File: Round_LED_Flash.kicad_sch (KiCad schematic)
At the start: 65 parts, among them J1 USB4085-GF-A, J2 BATTERY, Q20 AO3401A, Q21 AO3401A, Q22 2N7002-7-F, Q23 2N7002-7-F, SW1 POWER, SW2 SHUTTER, U10 ESP32-C3-WROOM-02-N4, U6 TPS63070RNMR

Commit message: Preserve balanced supercapacitor charger draft before completion
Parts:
- removed C31, C33: 5F 2.7V, Capacitor_THT:CP_Radial_D10.0mm_P5.00mm, symbol Device:C_Polarized
- removed R31, R32: 2.2k, Resistor_SMD:R_0603_1608Metric, symbol Device:R
- added C60: 4.7u 10V, Capacitor_SMD:C_0805_2012Metric, symbol Device:C
- added C61: 2.2u 16V, Capacitor_SMD:C_0805_2012Metric, symbol Device:C
- added Q30: AO3401A, Package_TO_SOT_SMD:SOT-23, symbol Transistor_FET:Q_PMOS_GSD
- added Q31, Q32, Q33: MMBT3904-7-F, Package_TO_SOT_SMD:SOT-23, symbol Transistor_BJT:Q_NPN_BEC
- added R52, R53, R60, R64, R65, R66, R67: 100k, Resistor_SMD:R_0603_1608Metric, symbol Device:R
- added R61: 24k, Resistor_SMD:R_0603_1608Metric, symbol Device:R
- added R62, R63: 10k, Resistor_SMD:R_0603_1608Metric, symbol Device:R
- added R68, R69: 47k, Resistor_SMD:R_0603_1608Metric, symbol Device:R
- added U30: LTC3225EDDB#TRMPBF, Package_DFN_QFN:DFN-10-1EP_2x3mm_P0.5mm_EP0.64x2.4mm, symbol Round_LED_Flash:LTC3225
- Q22, Q23: value 2N7002-7-F -> MMBT3904-7-F; symbol Transistor_FET:Q_NMOS_GSD -> Transistor_BJT:Q_NPN_BEC; BOM Comments Lifecycle/orderable suffix must be rechecked before BOM fre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 -> (none); MPN 2N7002-7-F -> MMBT3904-7-F
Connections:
- net 3V3: now also R62.1
- net ARM: now also R67.1
- net BAT_PROT: now also C60.1, Q30.2 (S), Q31.1 (B), R60.1, R67.2, U30.9 (VIN)
- net CAP_BANK: now also U30.10 (COUT)
- net CAP_MID: now also U30.3 (CX)
- net GND: now also C60.2, Q31.2 (E), Q32.2 (E), Q33.2 (E), R61.2, R64.2, R65.2, R66.2, U30.11 (EP_GND), U30.6 (VSEL), U30.8 (GND)
- net LOGIC_PG: now also R52.1, R53.1; no longer Q22.1 (G), Q23.1 (G)
- net VBUS_RAW: now also R65.1, R69.1
- new net CAP_CHG_EN: Q32.3 (C), Q33.3 (C), R63.2, R64.1, U30.4 (SHDN)
- new net CAP_EN_FEED: Q30.3 (D), R63.1
- new net CAP_EN_GATE: Q30.1 (G), Q31.3 (C), R60.2
- new net CAP_FLY_N: C61.2, U30.2 (C_MINUS)
- new net CAP_FLY_P: C61.1, U30.1 (C_PLUS)
- new net CAP_PGOOD: R62.2, U30.5 (PGOOD)
- new net CAP_PROG: R61.1, U30.7 (PROG)
- new net HW_WINDOW: R66.1, R68.1
- new net Q32_BASE: Q32.1 (B), R68.2
- new net Q33_BASE: Q33.1 (B), R69.2
- new net SENSE_BASE_0: Q22.1 (B), R52.2
- new net SENSE_BASE_1: Q23.1 (B), R53.2
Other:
- note added: "03 / 2.5 F EFFECTIVE CAP BANK - regulated 4.8 V"
- note added: "08 / 4.8 V SUPERCAP CHARGER + AUTOMATIC BALANCING"
- note added: "Charge enabled by ARM; USB presence or timed flash window forces SHDN low."
- note added: "Nominal stored energy 28.8 J. Flash isolation and service discharge still pending."
- note added: "Two series cells; midpoint connects to LTC3225 CX. No bleed balancing resistors."
- note added: "hardware pulse cutoff/re-arm, flash isolation/discharge, exact MPNs, routing,"
- note removed: "03 / 5 F EFFECTIVE CAP BANK - 5.4 V nominal rating"
- note removed: "INCOMPLETE: add limited reverse-blocking charger, per-section clamps and flash isolation."
- note removed: "Maximum charge is one protected Li-ion cell. Stored energy at 4.2 V = 44.1 J."
- note removed: "hardware pulse cutoff/re-arm, cap balancing/isolation, exact MPNs, routing,"

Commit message: Complete prototype circuit candidate with protected power and bounded flash control
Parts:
- added C1, C140, C141, C142, C143, C144, C145, C146, C147, C148, C149, C150, C151, C152, C153, C155, C156, C162, C163, C236, C273, C4, C5, C80, C9: 100n, Capacitor_SMD:C_0603_1608Metric, symbol Device:C
- added C2: 1u 50V, Capacitor_SMD:C_0805_2012Metric, symbol Device:C
- added C230, C231, C3: 1u 10V, Capacitor_SMD:C_0603_1608Metric, symbol Device:C
- added C270, C271, C272: 22u 10V, Capacitor_SMD:C_1206_3216Metric, symbol Device:C
- added C274, C283, C7: 100n 50V, Capacitor_SMD:C_0603_1608Metric, symbol Device:C
- added C275: 2.2u 10V, Capacitor_SMD:C_0805_2012Metric, symbol Device:C
- added C276: 10n, Capacitor_SMD:C_0603_1608Metric, symbol Device:C
- added C277: 33n, Capacitor_SMD:C_0603_1608Metric, symbol Device:C
- added C278: 47p, Capacitor_SMD:C_0603_1608Metric, symbol Device:C
- added C280, C281, C282: 10u 50V, Capacitor_SMD:C_1210_3225Metric, symbol Device:C
- added C284: 120u 35V, Capacitor_SMD:CP_Elec_10x12.6, symbol Device:C_Polarized
- added C6: 4.7u 16V, Capacitor_SMD:C_0805_2012Metric, symbol Device:C
- added C8: 10u 10V, Capacitor_SMD:C_0805_2012Metric, symbol Device:C
- added D1: RED, LED_SMD:LED_0603_1608Metric, symbol Device:LED
- added D4, D5: PESD5V0S1BA, Diode_SMD:D_SOD-323, symbol Device:D_TVS
- added D6: SMF4L6.0A, Diode_SMD:D_SOD-123F, symbol Device:D_TVS
- added D60: 10V ZENER, Diode_SMD:D_SOD-123, symbol Device:D_Zener
- added D70: GATE CLAMP, Diode_SMD:D_SOD-123, symbol Device:D
- added F1: 2A FAST, Fuse:Fuse_Littelfuse-NANO2-451_453, symbol Device:Fuse
- added F2: 7A FAST, Fuse:Fuse_Littelfuse-NANO2-451_453, symbol Device:Fuse
- added J3: BM02B-GHS-TBT(LF)(SN), Connector_JST:JST_GH_BM02B-GHS-TBT_1x02-1MP_P1.25mm_Vertical, symbol Round_LED_Flash:Pack_NTC_GH
- added J4: WARM COB, Connector_Wire:SolderWire-0.5sqmm_1x02_P4.6mm_D0.9mm_OD2.1mm, symbol Connector_Generic:Conn_01x02
- added J5: COOL COB, Connector_Wire:SolderWire-0.5sqmm_1x02_P4.6mm_D0.9mm_OD2.1mm, symbol Connector_Generic:Conn_01x02
- added L2: 1.5uH, Inductor_SMD:L_Coilcraft_XAL7030-152, symbol Device:L
- added LED1: BXRV-TR-2765G-10A0-A-23, symbol Round_LED_Flash:Vesta_Tunable_COB
- added Q1, Q2, Q34: AO3400A, Package_TO_SOT_SMD:SOT-23, symbol Transistor_FET:Q_NMOS_GSD
- added Q3, Q35, Q61, Q62: MMBT3904-7-F, Package_TO_SOT_SMD:SOT-23, symbol Transistor_BJT:Q_NPN_BEC
- added Q60: AO4407A, Package_SO:SOIC-8_3.9x4.9mm_P1.27mm, symbol Round_LED_Flash:AO4407A
- added Q70: SiR800DP-T1-GE3, Package_SO:PowerPAK_SO-8_Single, symbol Round_LED_Flash:SiR800DP
- added R1: 100, Resistor_SMD:R_0603_1608Metric, symbol Device:R
- added R100, R101, R232: 4.7k, Resistor_SMD:R_0603_1608Metric, symbol Device:R
- added R142: 165k, Resistor_SMD:R_0603_1608Metric, symbol Device:R
- added R143: 147k, Resistor_SMD:R_0603_1608Metric, symbol Device:R
- added R15, R233, R234: 2.2k, Resistor_SMD:R_0603_1608Metric, symbol Device:R
- added R152, R220, R221, R235, R240, R274, R70, R71, R8, R83, R84: 100k, Resistor_SMD:R_0603_1608Metric, symbol Device:R
- added R153, R162, R163, R18, R236, R237, R242, R272, R5, R7: 10k, Resistor_SMD:R_0603_1608Metric, symbol Device:R
- added R16, R17: 22, Resistor_SMD:R_0603_1608Metric, symbol Device:R
- added R164: 2.21M, Resistor_SMD:R_0603_1608Metric, symbol Device:R
- added R165, R81, R82: 1M, Resistor_SMD:R_0603_1608Metric, symbol Device:R
- added R2, R273: 1k, Resistor_SMD:R_0603_1608Metric, symbol Device:R
- added R200: 137k, Resistor_SMD:R_0603_1608Metric, symbol Device:R
- added R201: 240k, Resistor_SMD:R_0603_1608Metric, symbol Device:R
- added R210: 357k, Resistor_SMD:R_0603_1608Metric, symbol Device:R
- added R211: 146k, Resistor_SMD:R_0603_1608Metric, symbol Device:R
- added R230, R231: 2.49k, Resistor_SMD:R_0603_1608Metric, symbol Device:R
- added R238: 56k, Resistor_SMD:R_0603_1608Metric, symbol Device:R
- added R239: 261k, Resistor_SMD:R_0603_1608Metric, symbol Device:R
- added R241: 10M, Resistor_SMD:R_0603_1608Metric, symbol Device:R
- added R270: 0.010 0.5W, Resistor_SMD:R_0805_2012Metric, symbol Device:R
- added R271: 162k, Resistor_SMD:R_0603_1608Metric, symbol Device:R
- added R275: 120k, Resistor_SMD:R_0603_1608Metric, symbol Device:R
- added R276: 22k 0.125W, Resistor_SMD:R_0805_2012Metric, symbol Device:R
- added R3: 47k, Resistor_SMD:R_0603_1608Metric, symbol Device:R
- added R4: 887k, Resistor_SMD:R_0603_1608Metric, symbol Device:R
- added R6: 150k, Resistor_SMD:R_0603_1608Metric, symbol Device:R
- added R72, R73: 100 0.5W, Resistor_SMD:R_2010_5025Metric, symbol Device:R
- added R80: 6.49k, Resistor_SMD:R_0603_1608Metric, symbol Device:R
- added R9: 4.02k, Resistor_SMD:R_0603_1608Metric, symbol Device:R
- added TH2: 10k CELL NTC, symbol Device:Thermistor_NTC
- added TP7: CAP_BANK, TestPoint:TestPoint_Pad_D1.5mm, symbol Connector:TestPoint
- added TP8: CAP_MID, TestPoint:TestPoint_Pad_D1.5mm, symbol Connector:TestPoint
- added U1: DW01A, Package_TO_SOT_SMD:SOT-23-6, symbol Round_LED_Flash:DW01A
- added U2: TLV76033DBZR, Package_TO_SOT_SMD:SOT-23, symbol Round_LED_Flash:TLV76033
- added U3: TUSB320LAIRWBR, Package_DFN_QFN:Texas_X2QFN-12_1.6x1.6mm_P0.4mm, symbol Round_LED_Flash:TUSB320LAI
- added U4, U45: SN74LVC1G04DBVR, Package_TO_SOT_SMD:SOT-23-5, symbol Round_LED_Flash:SN74LVC1G04
- added U40, U41: LTC6993CS6-1#TRMPBF, Package_TO_SOT_SMD:SOT-23-6, symbol Round_LED_Flash:LTC6993_1
- added U42, U43, U55, U8: TLV3011BIDBVR, Package_TO_SOT_SMD:SOT-23-6, symbol Round_LED_Flash:TLV3011B
- added U44, U46, U47, U48, U49, U50, U51, U52, U53, U56: SN74LVC1G08DBVR, Package_TO_SOT_SMD:SOT-23-5, symbol Round_LED_Flash:SN74LVC1G08
- added U5: TPS25200DRVR, Package_SON:WSON-6-1EP_2x2mm_P0.65mm_EP1x1.6mm, symbol Round_LED_Flash:TPS25200
- added U54: TPS3808G33DBVR, Package_TO_SOT_SMD:SOT-23-6, symbol Round_LED_Flash:TPS3808G33
- added U60, U61: CAT4101TV-T75, Package_TO_SOT_SMD:TO-263-5_TabPin3, symbol Round_LED_Flash:CAT4101
- added U62, U63: SN74LVC1G125DBVR, Package_TO_SOT_SMD:SOT-23-5, symbol Round_LED_Flash:SN74LVC1G125
- added U7: TP4056-42-ESOP8, Round_LED_Flash:TP4056_TopPower_ESOP8, symbol Round_LED_Flash:TP4056
- added U70: MP3435GL-Z, Round_LED_Flash:MP3435_QFN20_3x4, symbol Round_LED_Flash:MP3435
- added U9: TPS3808G30DBVR, Package_TO_SOT_SMD:SOT-23-6, symbol Round_LED_Flash:TPS3808G30
- C10, C21, C23, C24, C40, C41: BOM Comments (none) -> Exact nominal/package selection; effective capacitance and 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; MPN (none) -> GRM188R71H104KA93D; Manufacturer (none) -> Murata
- C11, C12, C13, C22: BOM Comments (none) -> Exact nominal/package selection; effective capacitance and 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; MPN (none) -> GRM21BR61C106KE15L; Manufacturer (none) -> Murata
- C14, C15, C16: BOM Comments (none) -> Exact nominal/package selection; effective capacitance and 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; MPN (none) -> GRM21BR61C226ME44L; Manufacturer (none) -> Murata
- C20: BOM Comments (none) -> Exact nominal/package selection; effective capacitance and 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; MPN (none) -> GRM188R61C105KA12D; Manufacturer (none) -> Murata
- C60: BOM Comments (none) -> Exact nominal/package selection; effective capacitance and 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; MPN (none) -> GRM21BR71E475KA73L; Manufacturer (none) -> Murata
- C61: BOM Comments Select effective capacitance >=1uF at applied voltage for charge-pump flying capacitor. -> Select effective capacitance >=1uF at applied voltage for charge-pump flying capacitor. Exact nominal/package selection; effective capacitance and source verification pending.; MPN (none) -> GRM21BR71C225KA12L; Manufacturer (none) -> Murata
- D2: value BLUE -> AMBER BLE; MPN (none) -> LTST-C190KFKT; Manufacturer (none) -> Lite-On
- D3: MPN (none) -> LTST-C190KGKT; Manufacturer (none) -> Lite-On
- J2: BOM Comments Raw cell negative is not protected system ground. Fuse and 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 -> Raw cell negative is not protected system ground. Connect a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
- R10: BOM Comments (none) -> 1% general-purpose resistor; individual sourcing and series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; MPN (none) -> RC0603FR-07470KL; Manufacturer (none) -> Yageo
- R11: BOM Comments (none) -> 1% general-purpose resistor; individual sourcing and series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; MPN (none) -> RC0603FR-07150KL; Manufacturer (none) -> Yageo
- R12: value 10k -> 4.7k; BOM Comments (none) -> 1% general-purpose resistor; individual sourcing and series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; MPN (none) -> RC0603FR-074K7L; Manufacturer (none) -> Yageo
- R13: value 10k -> 100k; BOM Comments (none) -> 1% general-purpose resistor; individual sourcing and series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; MPN (none) -> RC0603FR-07100KL; Manufacturer (none) -> Yageo
- R14: value 100k -> 1M; BOM Comments (none) -> 1% general-purpose resistor; individual sourcing and series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; MPN (none) -> RC0603FR-071ML; Manufacturer (none) -> Yageo
- R20, R21, R22, R23, R40, R41, R62, R63: BOM Comments (none) -> 1% general-purpose resistor; individual sourcing and series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; MPN (none) -> RC0603FR-0710KL; Manufacturer (none) -> Yageo
- R24, R25, R26: BOM Comments Default-low flash/arm request. Hardware interlocks remain mandatory during boot/reset. -> Default-low flash/arm request. Hardware interlocks remain mandatory during boot/reset. 1% general-purpose resistor; individual sourcing and series-code audit pending.; MPN (none) -> RC0603FR-074K7L; Manufacturer (none) -> Yageo
- R27, R28, R29, R30, R50, R51, R60, R64, R65, R66, R67: BOM Comments (none) -> 1% general-purpose resistor; individual sourcing and series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; MPN (none) -> RC0603FR-07100KL; Manufacturer (none) -> Yageo
- R42, R43: BOM Comments (none) -> 1% general-purpose resistor; individual sourcing and series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; MPN (none) -> RC0603FR-071KL; Manufacturer (none) -> Yageo
- R52, R53: BOM Comments Base current limits PG loading; pull-down saturation current is only tens of microamps. -> Base current limits PG loading; pull-down saturation current is only tens of microamps. 1% general-purpose resistor; individual sourcing and series-code audit pending.; MPN (none) -> RC0603FR-07100KL; Manufacturer (none) -> Yageo
- R61: BOM Comments Nominal input current 150mA; nominal balanced bank charge current 75mA. -> Nominal input current 150mA; nominal balanced bank charge current 75mA. 1% general-purpose resistor; individual sourcing and series-code audit pending.; MPN (none) -> RC0603FR-0724KL; Manufacturer (none) -> Yageo
- R68, R69: BOM Comments (none) -> 1% general-purpose resistor; individual sourcing and series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; MPN (none) -> RC0603FR-0747KL; Manufacturer (none) -> Yageo
- TH1: MPN (none) -> NTCG163JF103FT1; Manufacturer (none) -> TDK
- TP3: value UART_TX -> UART_TX_EXT
- TP4: value UART_RX -> UART_RX_EXT
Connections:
- net 3V3: now also C140.1, C141.1, C142.1, C143.1, C144.1, C145.1, C146.1, C147.1, C148.1, C149.1, C150.1, C151.1, C152.1, C153.1, C155.1, C156.1, C162.1, C163.1, C230.1, C231.1, C236.1, R162.1, R163.1, R210.1, R211.1, R236.1, R237.1, R242.1, U40.5 (VDD), U41.5 (VDD), U42.6 (VDD), U43.6 (VDD), U44.5 (VCC), U45.5 (VCC), U46.5 (VCC), U47.5 (VCC), U48.5 (VCC), U49.5 (VCC), U50.5 (VCC), U51.5 (VCC), U52.5 (VCC), U53.5 (VCC), U54.5 (SENSE), U54.6 (VDD), U55.6 (VDD), U56.5 (VCC), U60.2 (VIN), U61.2 (VIN), U62.5 (VDD), U63.5 (VDD)
- net ARM: now also U47.2 (B)
- net BAT_PROT: now also C8.1, C9.1, F1.2, R1.1, R18.1, U7.5 (BAT), U9.3 (MR_N), U9.5 (SENSE), U9.6 (VDD); no longer U6.1 (PS_SYNC)
- net CAP_BANK: now also F2.1, R142.1, R239.1, R70.1, R72.1, R73.1, TP7.1
- net CAP_MID: now also TP8.1
- net CC1: now also R16.2, U3.1 (CC1); no longer J1.A5 (CC1)
- net CC2: now also R17.2, U3.2 (CC2); no longer J1.B5 (CC2)
- net CELL_N_RAW: now also C1.2, Q1.2 (S), U1.6 (VSS)
- net CELL_P: now also F1.1
- net GND: now also C140.2, C141.2, C142.2, C143.2, C144.2, C145.2, C146.2, C147.2, C148.2, C149.2, C150.2, C151.2, C152.2, C153.2, C155.2, C156.2, C162.2, C163.2, C2.2, C230.2, C231.2, C236.2, C270.2, C271.2, C272.2, C273.2, C275.2, C276.2, C278.2, C280.2, C281.2, C282.2, C283.2, C284.2, C3.2, C4.2, C5.2, C6.2, C7.2, C8.2, C80.2, C9.2, D4.1 (A1), D5.1 (A1), D6.2 (A2), J3.2 (GND), J3.MP (MOUNT), Q2.2 (S), Q3.2 (E), Q34.2 (S), Q35.2 (E), Q61.2 (E), Q62.2 (E), R100.2, R101.2, R152.2, R153.2, R2.1, R200.2, R201.2, R220.2, R221.2, R230.2, R231.2, R235.2, R240.2, R272.2, R274.2, R275.2, R276.2, R6.2, R8.2, R82.2, R84.2, R9.2, TH2.2, U2.3 (GND), U3.10 (GND), U3.11 (EN_N), U3.3 (PORT), U4.3 (GND), U40.2 (GND), U41.2 (GND), U42.2 (GND), U43.2 (GND), U44.3 (GND), U45.3 (GND), U46.3 (GND), U47.3 (GND), U48.3 (GND), U49.3 (GND), U5.5 (GND), U5.7 (EP), U50.3 (GND), U51.3 (GND), U52.3 (GND), U53.3 (GND), U54.2 (GND), U55.2 (GND), U56.3 (GND), U60.3 (GND_TAB), U61.3 (GND_TAB), U62.3 (GND), U63.3 (GND), U7.3 (GND), U7.9 (EP), U70.10 (PGND), U70.16 (AGND), U70.17 (PGND), U70.18 (PGND), U70.19 (PGND), U8.2 (GND), U9.2 (GND)
- net HW_OK: now also U48.4 (Y), U49.1 (A), U51.2 (B); no longer U10.6 (IO7)
- net HW_WINDOW: now also R234.1, U51.4 (Y), U52.2 (B), U53.2 (B)
- net LOGIC_PG: now also R71.1, U54.3 (MR_N)
- net REQ_C: now also U53.1 (A)
- net REQ_W: now also U52.1 (A)
- net SYS_EN: now also Q3.3 (C), U9.1 (RESET_N)
- net UART_RX: now also U62.4 (Y); no longer TP4.1
- net UART_TX: now also U63.2 (A); no longer TP3.1
- net VBUS_RAW: now also C2.1, C7.1, D6.1 (A1), R3.1, R4.1, U2.2 (IN), U5.6 (IN)
- net STRAP2 renamed TRIG_REQ
- net TRIG_REQ: now also U44.1 (A)
- new net BOOST_BST: C274.1, U70.4 (BST)
- new net BOOST_COMP: C277.1, C278.1, U70.13 (COMP)
- new net BOOST_COMP_R: C277.2, R275.1
- new net BOOST_EN: R273.2, R274.1, U70.6 (EN)
- new net BOOST_FB: R271.2, R272.1, U70.14 (FB)
- new net BOOST_INPUT: D70.2 (A), L2.1, Q70.1 (S), Q70.2 (S), Q70.3 (S)
- new net BOOST_INPUT_GATE: D70.1 (K), Q70.4 (G), U70.7 (GATE)
- new net BOOST_OK: R163.2, R165.1, U43.1 (OUT), U48.2 (B)
- new net BOOST_OUT: C280.1, C281.1, C282.1, C283.1, C284.1, D60.1 (K), Q60.1 (S), Q60.2 (S), Q60.3 (S), R143.1, R232.1, R271.1, R276.1, U70.1 (OUT), U70.2 (OUT), U70.5 (SOUT)
- new net BOOST_OUT_HW_REF: U43.4 (IN_MINUS), U43.5 (REF)
- new net BOOST_OUT_HW_SENSE: R143.2, R153.1, R165.2, U43.3 (IN_PLUS)
- new net BOOST_REQUEST: R273.1, U47.4 (Y), U48.1 (A)
- new net BOOST_SENSE: Q70.5 (D_5_6_7_8), R270.2, U70.8 (SENSE)
- new net BOOST_SS: C276.1, U70.15 (SS)
- new net BOOST_SW: C274.2, L2.2, U70.20 (SW), U70.9 (SW)
- new net BOOST_VDD: C275.1, U70.12 (VDD)
- new net CAP_BANK_HW_REF: U42.4 (IN_MINUS), U42.5 (REF)
- new net CAP_BANK_HW_SENSE: R142.2, R152.1, R164.2, U42.3 (IN_PLUS)
- new net CAP_DUMP_BASE: Q35.1 (B), R71.2
- new net CAP_DUMP_DRAIN: Q34.3 (D), R72.2, R73.2
- new net CAP_DUMP_GATE: Q34.1 (G), Q35.3 (C), R70.2
- new net CAP_FUSED: C270.1, C271.1, C272.1, C273.1, F2.2, R270.1, U70.11 (IN)
- new net CAP_OK: R162.2, R164.1, U42.1 (OUT), U46.2 (B)
- new net CAP_READY: R241.1, R242.2, U55.1 (OUT), U56.1 (A)
- new net CAP_READY_REF: U55.4 (IN_MINUS), U55.5 (REF)
- new net CAP_READY_SENSE: R239.2, R240.1, R241.2, U55.3 (IN_PLUS)
- new net CC1_RAW: D4.2 (A2), J1.A5 (CC1), R16.1
- new net CC2_RAW: D5.2 (A2), J1.B5 (CC2), R17.1
- new net CC_ALLOWED: R7.1, U4.4 (Y), U5.4 (EN)
- new net CC_CURRENT_N: R5.2, U3.7 (OUT1), U4.2 (A)
- new net CC_VBUS_DET: R4.2, U3.4 (VBUS_DET)
- new net CELL_CS: R2.2, U1.2 (CS)
- new net CELL_FET_COMMON: Q1.3 (D), Q2.3 (D)
- new net CELL_IC_VCC: C1.1, R1.2, U1.5 (VCC)
- new net CELL_OC: Q2.1 (G), U1.3 (OC)
- new net CELL_OD: Q1.1 (G), U1.1 (OD)
- new net CHARGE_ALLOWED: R7.2, R8.1, U7.8 (CE), U8.1 (OUT)
- new net CHARGE_PROG: R9.1, U7.2 (PROG)
- new net CHG_LED_A: D1.2 (A), R15.2
- new net CHRG_N: D1.1 (K), U7.7 (CHRG_N)
- new net COOLDOWN: U41.6 (OUT), U45.2 (A)
- new net COOLDOWN_READY: U45.4 (Y), U56.2 (B)
- new net C_ISET: R231.1, U61.4 (RSET)
- new net ENERGY_REARM_OK: U49.2 (B), U56.4 (Y)
- new net FLASH_TRIGGER: U40.1 (TRIG), U50.4 (Y)
- new net LED_ANODES: J4.1 (Pin_1), J5.1 (Pin_1), LED1.1 (W_PLUS), LED1.3 (C_PLUS), Q60.5 (D), Q60.6 (D), Q60.7 (D), Q60.8 (D)
- new net LED_C_K: J5.2 (Pin_2), LED1.4 (C_MINUS), U61.5 (LED)
- new net LED_GATE_BASE: Q61.1 (B), R234.2, R235.1
- new net LED_GATE_PULL: Q61.3 (C), R233.2
- new net LED_POWER_GATE: D60.2 (A), Q60.4 (G), R232.2, R233.1
- new net LED_W_K: J4.2 (Pin_2), LED1.2 (W_MINUS), U60.5 (LED)
- new net LOGIC_PS_SYNC: R18.2, U6.1 (PS_SYNC)
- new net PACK_TEMP: J3.1 (NTC), R80.2, R81.1, TH2.1, U7.1 (TEMP)
- new net PACK_TEMP_HALF: R81.2, R82.1, U8.3 (IN_PLUS)
- new net POR_OK: R236.2, R238.1, U44.2 (B), U46.1 (A), U54.1 (RESET_N)
- new net RAILS_OK: U46.4 (Y), U47.1 (A)
- new net SINK_C_EN: R101.1, U53.4 (Y), U61.1 (EN_PWM)
- new net SINK_W_EN: R100.1, U52.4 (Y), U60.1 (EN_PWM)
- new net TEMP_REF: R83.1, U8.5 (REF)
- new net TEMP_REF_HALF: R83.2, R84.1, U8.4 (IN_MINUS)
- new net TIMER_WINDOW: U40.6 (OUT), U41.1 (TRIG), U51.1 (A)
- new net TRIGGER_ALLOWED: U10.6 (IO7), U49.4 (Y), U50.2 (B)
- new net TRIG_SAFE: U44.4 (Y), U50.1 (A)
- new net U40_DIV: R210.2, R220.1, U40.4 (DIV)
- new net U40_SET: R200.1, U40.3 (SET)
- new net U41_DIV: R211.2, R221.1, U41.4 (DIV)
- new net U41_SET: R201.1, U41.3 (SET)
- new net UART_ENABLE_BASE: Q62.1 (B), R238.2
- new net UART_OE_N: Q62.3 (C), R237.2, U62.1 (OE_N), U63.1 (OE_N)
- new net UART_RX_EXT: TP4.1, U62.2 (A)
- new net UART_TX_EXT: TP3.1, U63.4 (Y)
- new net USB_3V3: C3.1, C4.1, C5.1, C80.1, R5.1, U2.1 (OUT), U3.12 (VDD), U4.5 (VCC), U8.6 (VDD)
- new net USB_5V: C6.1, R15.1, R80.1, U5.1 (OUT), U7.4 (VCC)
- new net USB_ILIM: R6.1, U5.2 (ILIM)
- new net USB_INHIBIT_BASE: Q3.1 (B), R3.2
- new net W_ISET: R230.1, U60.4 (RSET)
- no-connect marks 7 -> 19
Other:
- note added: "09 / CELL FUSE + DW01 LOW-SIDE PROTECTION"
- note added: "10 / TYPE-C SOURCE QUALIFICATION - CHARGING ONLY"
- note added: "11 / PROTECTED VBUS + 300 mA CELL CHARGER"
- note added: "12 / CELL NTC + SHORTED-SENSOR INHIBIT"
- note added: "13 / DEFAULT-ON CAPACITOR SERVICE DISCHARGE"
- note added: "14 / INDEPENDENT RAIL INTERLOCKS"
- note added: "15 / NON-RETRIGGERABLE PULSE + COOLDOWN"
- note added: "16 / HARDWARE FLASH PERMISSION + CHANNEL GATING"
- note added: "17 / PHYSICAL LED POWER CUTOFF - DEFAULT OFF"
- note added: "18 / 21.07 V BOOST + INPUT DISCONNECT / CURRENT LIMIT"
- note added: "19 / POWER-ON DELAY + Ioff UART ISOLATION"
- note added: "20 / PRE-FLASH ENERGY QUALIFICATION"
- note added: "Charging disables logic and cap recharge in hardware. Ground is protected pack negative."
- note added: "D1 indicates battery charging; D2 BLE; D3 firmware flash-ready. TH1 senses LED-area temperature."
- note added: "Default-current and legacy USB sources do not charge this implementation."
- note added: "External COB: BXRV-TR-2765G-10A0-A-23, independent channels, bonded heat spreader."
- note added: "GPIO2 high for boot, then TRIG_REQ output LOW before ARM. GPIO7 reads TRIGGER_ALLOWED."
- note added: "Loaded-rail interlocks: cap ~3.39V rising / 3.15V falling; boost ~19.67V / 19.20V."
- note added: "Nominal bank discharge to 0.5V takes about 4.8 minutes; measure before handling."
- note added: "Nominal cap-ready ~4.51V rising / 4.43V falling. Pulse sag is handled by U42 UVLO."
- note added: "Nominal stored energy 28.8 J. Fused boost branch, timed output cutoff and default-on discharge."
- note added: "Open sensor inhibits through TP4056; short inhibits through U8. Check startup and thresholds."
- note added: "Output reservoir is BEFORE physical cutoff. Never add bulk capacitance on LED_ANODES."
- note added: "Raw negative is isolated from all USB, fixture and enclosure grounds."
- note added: "U40: 1.403ms nominal maximum window; U41: 1.258s lockout from each window start."
- note removed: "06 / RELEASE STATUS: ENGINEERING DRAFT"
- note removed: "Boot GPIO2/8 high; GPIO9 high for normal boot, low at reset for UART download."
- note removed: "Nominal stored energy 28.8 J. Flash isolation and service discharge still pending."
- note removed: "One authoritative schematic/PCB/project. No fabrication release."
- note removed: "PCB geometry: 84 mm OD / 55 mm opening / 4 layers / 1.6 mm FR4."
- note removed: "Pending: USB current detection, TP4056, DW01, cell NTC, flash boost and sinks,"
- note removed: "USB charge-status LED belongs in the pending charger block."
- note removed: "electrical/thermal/EMC verification and manufacturing outputs."
- note removed: "hardware pulse cutoff/re-arm, flash isolation/discharge, exact MPNs, routing,"

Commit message: Correct service bleed and ADC leakage; refine converter and decoupling placement
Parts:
- added R74: 330 0.25W, Resistor_SMD:R_1206_3216Metric, symbol Device:R
- R27, R28, R29, R30: value 100k -> 22k; MPN RC0603FR-07100KL -> RC0603FR-0722KL
- R72, R73: BOM Comments Parallel 50ohm discharge, 0.48W initial total at 4.9V. Effe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 -> Parallel 50ohm active dump, 0.48W initial total at 4.9V. Sl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
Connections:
- net CAP_BANK: now also R74.1
- net GND: now also R74.2
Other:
- note added: "Active dump removes most energy; permanent 330ohm bleed provides final discharge. Measure TP7 before service."
- note removed: "Nominal bank discharge to 0.5V takes about 4.8 minutes; measure before handling."
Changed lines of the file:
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@@
 (in_bom yes) (on_board yes) (dnp no)
 (property "Reference" "R27" (at 389.89 120.46000000000001 0)  (effects (font (size 0.9 0.9)) ))
-(property "Value" "100k" (at 389.89 122.66000000000001 0)  (effects (font (size 0.9 0.9)) ))
+(property "Value" "22k" (at 389.89 122.66000000000001 0)  (effects (font (size 0.9 0.9)) ))
 (property "Footprint" "Resistor_SMD:R_0603_1608Metric" (at 389.89 122.66000000000001 0) (hide yes) (effects (font (size 0.9 0.9)) ))
 (property "Datasheet" "" (at 389.89 122.66000000000001 0) (hide yes) (effects (font (size 0.9 0.9)) ))
-(property "MPN" "RC0603FR-07100KL" (at 389.89 122.66000000000001 0) (hide yes) (effects (font (size 0.9 0.9)) ))
+(property "MPN" "RC0603FR-0722KL" (at 389.89 122.66000000000001 0) (hide yes) (effects (font (size 0.9 0.9)) ))
 (property "Manufacturer" "Yageo" (at 389.89 122.66000000000001 0) (hide yes) (effects (font (size 0.9 0.9)) ))
 (property "BOM Comments" " 1% general-purpose resistor; individual sourcing and series-code audit pending." (at 389.89 122.66000000000001 0) (hide yes) (effects (font (size 0.9 0.9)) ))
@@
 (in_bom yes) (on_board yes) (dnp no)
 (property "Reference" "R28" (at 439.42 120.46000000000001 0)  (effects (font (size 0.9 0.9)) ))
-(property "Value" "100k" (at 439.42 122.66000000000001 0)  (effects (font (size 0.9 0.9)) ))
+(property "Value" "22k" (at 439.42 122.66000000000001 0)  (effects (font (size 0.9 0.9)) ))
 (property "Footprint" "Resistor_SMD:R_0603_1608Metric" (at 439.42 122.66000000000001 0) (hide yes) (effects (font (size 0.9 0.9)) ))
 (property "Datasheet" "" (at 439.42 122.66000000000001 0) (hide yes) (effects (font (size 0.9 0.9)) ))
-(property "MPN" "RC0603FR-07100KL" (at 439.42 122.66000000000001 0) (hide yes) (effects (font (size 0.9 0.9)) ))
+(property "MPN" "RC0603FR-0722KL" (at 439.42 122.66000000000001 0) (hide yes) (effects (font (size 0.9 0.9)) ))
 (property "Manufacturer" "Yageo" (at 439.42 122.66000000000001 0) (hide yes) (effects (font (size 0.9 0.9)) ))
 (property "BOM Comments" " 1% general-purpose resistor; individual sourcing and series-code audit pending." (at 439.42 122.66000000000001 0) (hide yes) (effects (font (size 0.9 0.9)) ))
@@
 (in_bom yes) (on_board yes) (dnp no)
 (property "Reference" "R29" (at 389.89 140.78 0)  (effects (font (size 0.9 0.9)) ))
-(property "Value" "100k" (at 389.89 142.98 0)  (effects (font (size 0.9 0.9)) ))
+(property "Value" "22k" (at 389.89 142.98 0)  (effects (font (size 0.9 0.9)) ))
 (property "Footprint" "Resistor_SMD:R_0603_1608Metric" (at 389.89 142.98 0) (hide yes) (effects (font (size 0.9 0.9)) ))
 (property "Datasheet" "" (at 389.89 142.98 0) (hide yes) (effects (font (size 0.9 0.9)) ))
-(property "MPN" "RC0603FR-07100KL" (at 389.89 142.98 0) (hide yes) (effects (font (size 0.9 0.9)) ))
+(property "MPN" "RC0603FR-0722KL" (at 389.89 142.98 0) (hide yes) (effects (font (size 0.9 0.9)) ))
 (property "Manufacturer" "Yageo" (at 389.89 142.98 0) (hide yes) (effects (font (size 0.9 0.9)) ))
 (property "BOM Comments" " 1% general-purpose resistor; individual sourcing and series-code audit pending." (at 389.89 142.98 0) (hide yes) (effects (font (size 0.9 0.9)) ))
@@
 (in_bom yes) (on_board yes) (dnp no)
 (property "Reference" "R30" (at 439.42 140.78 0)  (effects (font (size 0.9 0.9)) ))
-(property "Value" "100k" (at 439.42 142.98 0)  (effects (font (size 0.9 0.9)) ))
+(property "Value" "22k" (at 439.42 142.98 0)  (effects (font (size 0.9 0.9)) ))
 (property "Footprint" "Resistor_SMD:R_0603_1608Metric" (at 439.42 142.98 0) (hide yes) (effects (font (size 0.9 0.9)) ))
 (property "Datasheet" "" (at 439.42 142.98 0) (hide yes) (effects (font (size 0.9 0.9)) ))
-(property "MPN" "RC0603FR-07100KL" (at 439.42 142.98 0) (hide yes) (effects (font (size 0.9 0.9)) ))
+(property "MPN" "RC0603FR-0722KL" (at 439.42 142.98 0) (hide yes) (effects (font (size 0.9 0.9)) ))
 (property "Manufacturer" "Yageo" (at 439.42 142.98 0) (hide yes) (effects (font (size 0.9 0.9)) ))
 (property "BOM Comments" " 1% general-purpose resistor; individual sourcing and series-code audit pending." (at 439.42 142.98 0) (hide yes) (effects (font (size 0.9 0.9)) ))
@@
 (property "MPN" "RC2010FK-07100RL" (at 929.64 503.65999999999997 0) (hide yes) (effects (font (size 0.9 0.9)) ))
 (property "Manufacturer" "Yageo" (at 929.64 503.65999999999997 0) (hide yes) (effects (font (size 0.9 0.9)) ))
-(property "BOM Comments" "Parallel 50ohm discharge, 0.48W initial total at 4.9V. Effective 2.5F: nominal 125s time constant. 1% general-purpose resistor; individual sourcing and series-code audit pending." (at 929.64 503.65999999999997 0) (hide yes) (effects (font (size 0.9 0.9)) ))
+(property "BOM Comments" "Parallel 50ohm active dump, 0.48W initial total at 4.9V. Slows near MOSFET threshold; R74 provides final bleed. 1% general-purpose resistor; individual sourcing and series-code audit pending." (at 929.64 503.65999999999997 0) (hide yes) (effects (font (size 0.9 0.9)) ))
 (property "Design_Status" "DRAFT - UNRELEASED" (at 929.64 503.65999999999997 0) (hide yes) (effects (font (size 0.9 0.9)) ))
 (pin "1")
@@
 (property "MPN" "RC2010FK-07100RL" (at 980.44 503.65999999999997 0) (hide yes) (effects (font (size 0.9 0.9)) ))
 (property "Manufacturer" "Yageo" (at 980.44 503.65999999999997 0) (hide yes) (effects (font (size 0.9 0.9)) ))
-(property "BOM Comments" "Parallel 50ohm discharge, 0.48W initial total at 4.9V. Effective 2.5F: nominal 125s time constant. 1% general-purpose resistor; individual sourcing and series-code audit pending." (at 980.44 503.65999999999997 0) (hide yes) (effects (font (size 0.9 0.9)) ))
+(property "BOM Comments" "Parallel 50ohm active dump, 0.48W initial total at 4.9V. Slows near MOSFET threshold; R74 provides final bleed. 1% general-purpose resistor; individual sourcing and series-code audit pending." (at 980.44 503.65999999999997 0) (hide yes) (effects (font (size 0.9 0.9)) ))
 (property "Design_Status" "DRAFT - UNRELEASED" (at 980.44 503.65999999999997 0) (hide yes) (effects (font (size 0.9 0.9)) ))
 (pin "1")
@@
 (instances (project "Round_LED_Flash" (path "/6912c85e-f5ae-5f10-8ede-7dd6d69a605d" (reference "R73") (unit 1))))
 )
+(wire (pts (xy 1026.1600 505.4600) (xy 1023.6200 505.4600)) (stroke (width 0) (type default)))
+(label "CAP_BANK" (at 1023.6200 505.4600 180) (effects (font (size 0.9 0.9)) (justify left bottom)))
+(wire (pts (xy 1033.7800 505.4600) (xy 1036.3200 505.4600)) (stroke (width 0) (type default)))
+(label "GND" (at 1036.3200 505.4600 0) (effects (font (size 0.9 0.9)) (justify left bottom)))
+(symbol
+(lib_id "Device:R") (at 1029.97 505.46 90) (unit 1)
+(in_bom yes) (on_board yes) (dnp no)
+(property "Reference" "R74" (at 1029.97 501.46 0)  (effects (font (size 0.9 0.9)) ))
+(property "Value" "330 0.25W" (at 1029.97 503.65999999999997 0)  (effects (font (size 0.9 0.9)) ))
+(property "Footprint" "Resistor_SMD:R_1206_3216Metric" (at 1029.97 503.65999999999997 0) (hide yes) (effects (font (size 0.9 0.9)) ))
+(property "Datasheet" "" (at 1029.97 503.65999999999997 0) (hide yes) (effects (font (size 0.9 0.9)) ))
+(property "MPN" "RC1206FR-07330RL" (at 1029.97 503.65999999999997 0) (hide yes) (effects (font (size 0.9 0.9)) ))
+(property "Manufacturer" "Yageo" (at 1029.97 503.65999999999997 0) (hide yes) (effects (font (size 0.9 0.9)) ))
+(property "BOM Comments" "Permanent bleeder: 73mW maximum at 4.9V. Conservative RC model below 0.5V within 60min; always measure TP7 before service. 1% general-purpose resistor; individual sourcing and series-code audit pending." (at 1029.97 503.65999999999997 0) (hide yes) (effects (font (size 0.9 0.9)) ))
+(property "Design_Status" "DRAFT - UNRELEASED" (at 1029.97 503.65999999999997 0) (hide yes) (effects (font (size 0.9 0.9)) ))
+(pin "1")
+(pin "2")
+(instances (project "Round_LED_Flash" (path "/6912c85e-f5ae-5f10-8ede-7dd6d69a605d" (reference "R74") (unit 1))))
+)
 (wire (pts (xy 929.6400 554.9900) (xy 929.6400 557.5300)) (stroke (width 0) (type default)))
 (label "CAP_BANK" (at 929.6400 557.5300 180) (effects (font (size 0.9 0.9)) (justify left bottom)))
@@
 (text "Open sensor inhibits through TP4056; short inhibits through U8. Check startup and thresholds." (at 545 605 0) (effects (font (size 1.2 1.2)) (justify left)))
 (text "13 / DEFAULT-ON CAPACITOR SERVICE DISCHARGE" (at 795 435 0) (effects (font (size 2 2)) (justify left)))
-(text "Nominal bank discharge to 0.5V takes about 4.8 minutes; measure before handling." (at 795 605 0) (effects (font (size 1.2 1.2)) (justify left)))
+(text "Active dump removes most energy; permanent 330ohm bleed provides final discharge. Measure TP7 before service." (at 795 605 0) (effects (font (size 1.2 1.2)) (justify left)))
 (text "14 / INDEPENDENT RAIL INTERLOCKS" (at 25 625 0) (effects (font (size 2 2)) (justify left)))
 (text "Loaded-rail interlocks: cap ~3.39V rising / 3.15V falling; boost ~19.67V / 19.20V." (at 25 805 0) (effects (font (size 1.2 1.2)) (justify left)))

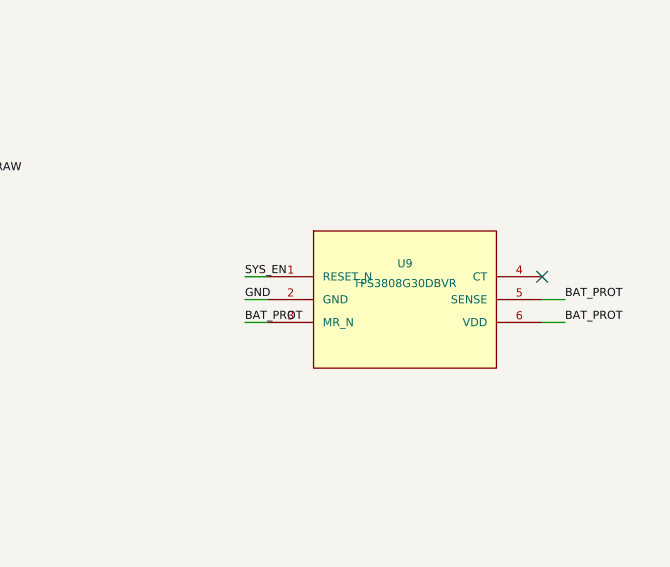
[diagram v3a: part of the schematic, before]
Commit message: Update Round LED Flash schematic, layout, routing scripts, and documentation
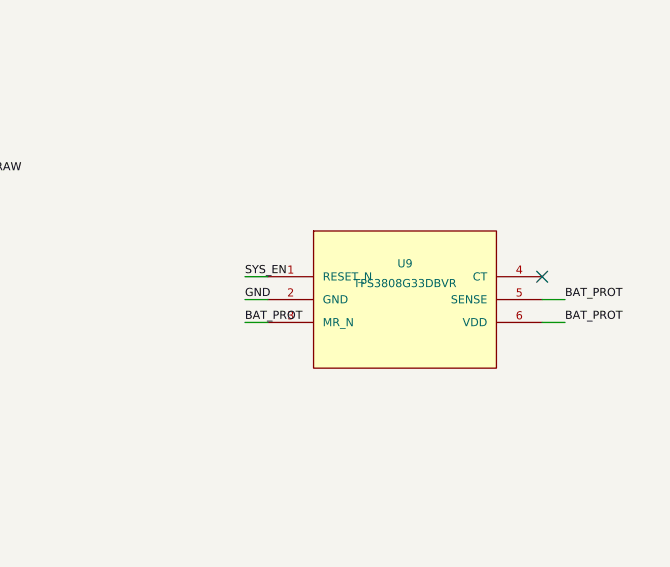
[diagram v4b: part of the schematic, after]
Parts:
- U9: value TPS3808G30DBVR -> TPS3808G33DBVR; symbol Round_LED_Flash:TPS3808G30 -> Round_LED_Flash:TPS3808G33; BOM Comments Independent 2.79V system undervoltage cutoff, before emerge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 -> Independent 3.07V system undervoltage cutoff; minimum thres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; MPN TPS3808G30DBVR -> TPS3808G33DBVR
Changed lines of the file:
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@@
 (label "BAT_PROT" (at 1097.2800 242.5700 0) (effects (font (size 0.9 0.9)) (justify left bottom)))
 (symbol
-(lib_id "Round_LED_Flash:TPS3808G30") (at 1079.5 240.03 0) (unit 1)
+(lib_id "Round_LED_Flash:TPS3808G33") (at 1079.5 240.03 0) (unit 1)
 (in_bom yes) (on_board yes) (dnp no)
 (property "Reference" "U9" (at 1079.5 236.03 0)  (effects (font (size 0.9 0.9)) ))
-(property "Value" "TPS3808G30DBVR" (at 1079.5 238.23 0)  (effects (font (size 0.9 0.9)) ))
+(property "Value" "TPS3808G33DBVR" (at 1079.5 238.23 0)  (effects (font (size 0.9 0.9)) ))
 (property "Footprint" "Package_TO_SOT_SMD:SOT-23-6" (at 1079.5 238.23 0) (hide yes) (effects (font (size 0.9 0.9)) ))
 (property "Datasheet" "https://www.ti.com/lit/ds/symlink/tps3808.pdf" (at 1079.5 238.23 0) (hide yes) (effects (font (size 0.9 0.9)) ))
-(property "MPN" "TPS3808G30DBVR" (at 1079.5 238.23 0) (hide yes) (effects (font (size 0.9 0.9)) ))
+(property "MPN" "TPS3808G33DBVR" (at 1079.5 238.23 0) (hide yes) (effects (font (size 0.9 0.9)) ))
 (property "Manufacturer" "Texas Instruments" (at 1079.5 238.23 0) (hide yes) (effects (font (size 0.9 0.9)) ))
-(property "BOM Comments" "Independent 2.79V system undervoltage cutoff, before emergency DW01 overdischarge. CT open gives nominal 20ms release delay." (at 1079.5 238.23 0) (hide yes) (effects (font (size 0.9 0.9)) ))
+(property "BOM Comments" "Independent 3.07V system undervoltage cutoff; minimum threshold remains above 3V converter startup requirement. CT open gives nominal 20ms release delay." (at 1079.5 238.23 0) (hide yes) (effects (font (size 0.9 0.9)) ))
 (property "Design_Status" "DRAFT - UNRELEASED" (at 1079.5 238.23 0) (hide yes) (effects (font (size 0.9 0.9)) ))
 (pin "1")
